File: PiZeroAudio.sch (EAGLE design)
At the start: 66 parts, among them CON1 RPI-ZERO, J1 GROVE, J2 2X2HEADER, J3 2X1-LOCKING, J4 4X1-LOCKING, Q1 DMG2305UX, U1 TXB0104PWR, U2 LSM6DS33, U3 NC7WZ16, U4 DMMT5401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

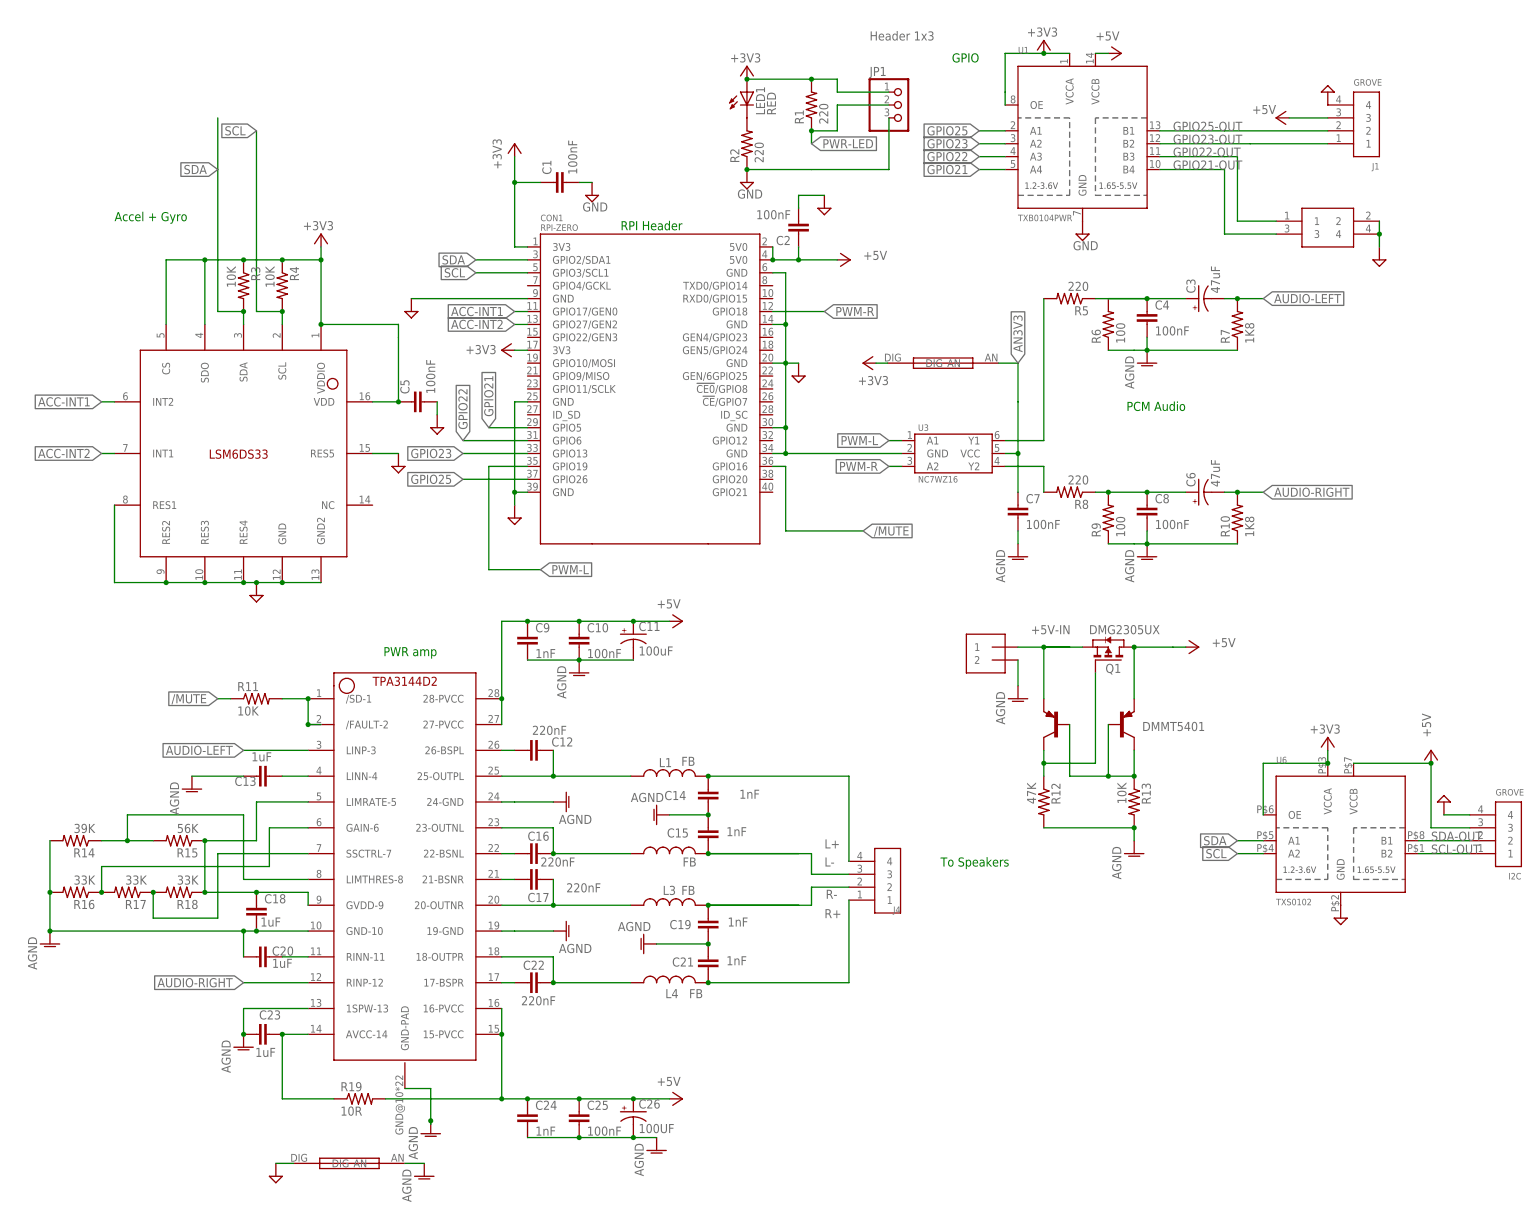
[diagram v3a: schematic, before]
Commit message: Changed capacitor footprints
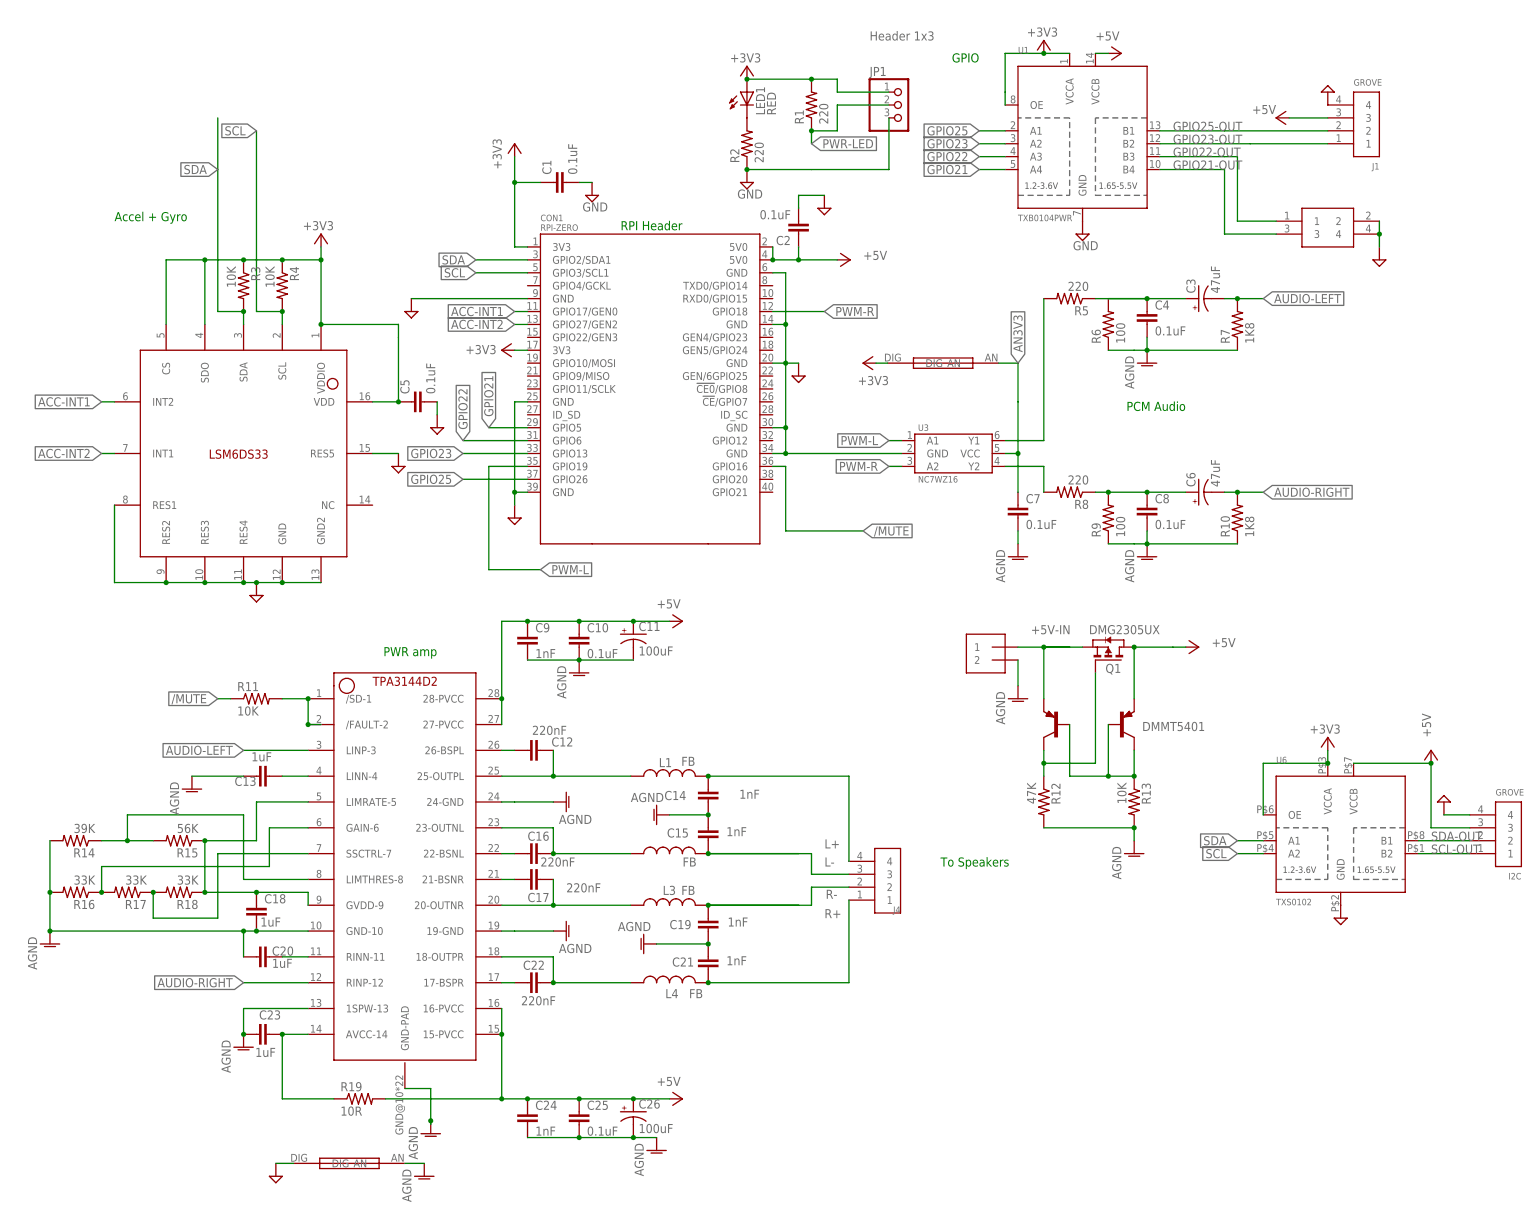
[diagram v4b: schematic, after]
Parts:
- C1, C10, C2, C25, C4, C5, C7, C8: value 100nF -> 0.1uF
- C11, C3, C6: device adafruit:CPOL-USCT3528 -> HappyBrackets:CAP-POLARISED
- C26: value 100UF -> 100uF; device adafruit:CPOL-USCT3528 -> HappyBrackets:CAP-POLARISED
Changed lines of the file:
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@@
 <layer number="112" name="tSilk" color="7" fill="1" visible="yes" active="yes"/>
 <layer number="113" name="IDFDebug" color="7" fill="1" visible="yes" active="yes"/>
+<layer number="114" name="Badge_Outline" color="7" fill="1" visible="no" active="no"/>
+<layer number="115" name="ReferenceISLANDS" color="7" fill="1" visible="no" active="no"/>
 <layer number="116" name="Patch_BOT" color="7" fill="1" visible="yes" active="yes"/>
 <layer number="117" name="mPads" color="7" fill="1" visible="yes" active="yes"/>
@@
 <parts>
 <part name="CON1" library="RPI-Zero" deviceset="RPI-ZERO" device=""/>
-<part name="C4" library="rcl" library_urn="urn:adsk.eagle:library:334" deviceset="C-EU" device="C0603" package3d_urn="urn:adsk.eagle:package:23616/2" value="100nF"/>
-<part name="C8" library="rcl" library_urn="urn:adsk.eagle:library:334" deviceset="C-EU" device="C0603" package3d_urn="urn:adsk.eagle:package:23616/2" value="100nF"/>
-<part name="C3" library="adafruit" deviceset="CPOL-US" device="CT3528" value="47uF"/>
-<part name="C6" library="adafruit" deviceset="CPOL-US" device="CT3528" value="47uF"/>
+<part name="C4" library="rcl" library_urn="urn:adsk.eagle:library:334" deviceset="C-EU" device="C0603" package3d_urn="urn:adsk.eagle:package:23616/2" value="0.1uF"/>
+<part name="C8" library="rcl" library_urn="urn:adsk.eagle:library:334" deviceset="C-EU" device="C0603" package3d_urn="urn:adsk.eagle:package:23616/2" value="0.1uF"/>
+<part name="C3" library="HappyBrackets" library_urn="urn:adsk.eagle:library:5224691" deviceset="CAP-POLARISED" device="" value="47uF"/>
+<part name="C6" library="HappyBrackets" library_urn="urn:adsk.eagle:library:5224691" deviceset="CAP-POLARISED" device="" value="47uF"/>
 <part name="R5" library="adafruit" deviceset="R-US_" device="R0603" value="220"/>
 <part name="R6" library="adafruit" deviceset="R-US_" device="R0603" value="100"/>
@@
 <part name="P+3" library="supply1" library_urn="urn:adsk.eagle:library:371" deviceset="+5V" device=""/>
 <part name="U3" library="fairchild" deviceset="NC7WZ16" device=""/>
-<part name="C7" library="rcl" library_urn="urn:adsk.eagle:library:334" deviceset="C-EU" device="C0603" package3d_urn="urn:adsk.eagle:package:23616/2" value="100nF"/>
+<part name="C7" library="rcl" library_urn="urn:adsk.eagle:library:334" deviceset="C-EU" device="C0603" package3d_urn="urn:adsk.eagle:package:23616/2" value="0.1uF"/>
 <part name="+3V33" library="supply1" library_urn="urn:adsk.eagle:library:371" deviceset="+3V3" device=""/>
 <part name="R7" library="adafruit" deviceset="R-US_" device="R0603" value="1K8"/>
 <part name="R10" library="adafruit" deviceset="R-US_" device="R0603" value="1K8"/>
 <part name="U2" library="HappyBrackets" library_urn="urn:adsk.eagle:library:5224691" deviceset="LSM6DS33" device="LGA-16-3X3" package3d_urn="urn:adsk.eagle:package:5224694/1" value="LSM6DS33"/>
-<part name="C5" library="rcl" library_urn="urn:adsk.eagle:library:334" deviceset="C-EU" device="C0603" package3d_urn="urn:adsk.eagle:package:23616/2" value="100nF"/>
+<part name="C5" library="rcl" library_urn="urn:adsk.eagle:library:334" deviceset="C-EU" device="C0603" package3d_urn="urn:adsk.eagle:package:23616/2" value="0.1uF"/>
 <part name="+3V34" library="supply1" library_urn="urn:adsk.eagle:library:371" deviceset="+3V3" device=""/>
-<part name="C1" library="rcl" library_urn="urn:adsk.eagle:library:334" deviceset="C-EU" device="C0603" package3d_urn="urn:adsk.eagle:package:23616/2" value="100nF"/>
+<part name="C1" library="rcl" library_urn="urn:adsk.eagle:library:334" deviceset="C-EU" device="C0603" package3d_urn="urn:adsk.eagle:package:23616/2" value="0.1uF"/>
 <part name="SUPPLY3" library="supply2" library_urn="urn:adsk.eagle:library:372" deviceset="GND" device=""/>
 <part name="R3" library="adafruit" deviceset="R-US_" device="R0603" value="10K"/>
@@
 <part name="SUPPLY9" library="supply2" library_urn="urn:adsk.eagle:library:372" deviceset="GND" device=""/>
 <part name="SUPPLY12" library="supply2" library_urn="urn:adsk.eagle:library:372" deviceset="GND" device=""/>
-<part name="C2" library="rcl" library_urn="urn:adsk.eagle:library:334" deviceset="C-EU" device="C0603" package3d_urn="urn:adsk.eagle:package:23616/2" value="100nF"/>
+<part name="C2" library="rcl" library_urn="urn:adsk.eagle:library:334" deviceset="C-EU" device="C0603" package3d_urn="urn:adsk.eagle:package:23616/2" value="0.1uF"/>
 <part name="SUPPLY4" library="supply2" library_urn="urn:adsk.eagle:library:372" deviceset="GND" device=""/>
 <part name="U1" library="adafruit" deviceset="TXB0104PWR" device="" value="TXB0104PWR"/>
@@
 <part name="U5" library="HappyBrackets" library_urn="urn:adsk.eagle:library:5224691" deviceset="TPA3144D2PWPR" device="" package3d_urn="urn:adsk.eagle:package:39216/1"/>
 <part name="P+4" library="supply1" library_urn="urn:adsk.eagle:library:371" deviceset="+5V" device=""/>
-<part name="C10" library="rcl" library_urn="urn:adsk.eagle:library:334" deviceset="C-EU" device="C0603" package3d_urn="urn:adsk.eagle:package:23616/2" value="100nF"/>
-<part name="C11" library="adafruit" deviceset="CPOL-US" device="CT3528" value="100uF"/>
+<part name="C10" library="rcl" library_urn="urn:adsk.eagle:library:334" deviceset="C-EU" device="C0603" package3d_urn="urn:adsk.eagle:package:23616/2" value="0.1uF"/>
+<part name="C11" library="HappyBrackets" library_urn="urn:adsk.eagle:library:5224691" deviceset="CAP-POLARISED" device="" value="100uF"/>
 <part name="R11" library="adafruit" deviceset="R-US_" device="R0603" value="10K"/>
 <part name="C13" library="rcl" library_urn="urn:adsk.eagle:library:334" deviceset="C-EU" device="C0603" package3d_urn="urn:adsk.eagle:package:23616/2" value="1uF"/>
@@
 <part name="R19" library="adafruit" deviceset="R-US_" device="R0603" value="10R"/>
 <part name="P+6" library="supply1" library_urn="urn:adsk.eagle:library:371" deviceset="+5V" device=""/>
-<part name="C25" library="rcl" library_urn="urn:adsk.eagle:library:334" deviceset="C-EU" device="C0603" package3d_urn="urn:adsk.eagle:package:23616/2" value="100nF"/>
-<part name="C26" library="adafruit" deviceset="CPOL-US" device="CT3528" value="100UF"/>
+<part name="C25" library="rcl" library_urn="urn:adsk.eagle:library:334" deviceset="C-EU" device="C0603" package3d_urn="urn:adsk.eagle:package:23616/2" value="0.1uF"/>
+<part name="C26" library="HappyBrackets" library_urn="urn:adsk.eagle:library:5224691" deviceset="CAP-POLARISED" device="" value="100uF"/>
 <part name="C24" library="rcl" library_urn="urn:adsk.eagle:library:334" deviceset="C-EU" device="C0603" package3d_urn="urn:adsk.eagle:package:23616/2" value="1nF"/>
 <part name="L1" library="HappyBrackets" library_urn="urn:adsk.eagle:library:5224691" deviceset="NFZ2MSM" device="L0806" package3d_urn="urn:adsk.eagle:package:32724/1" value="FB"/>

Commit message: Changed Capacitor sizes for tant caps
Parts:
- C11, C26, C3, C6: device HappyBrackets:CAP-POLARISED -> HappyBrackets:CAP-POLARISED1206-POLAR
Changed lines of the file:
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@@
 <part name="C4" library="rcl" library_urn="urn:adsk.eagle:library:334" deviceset="C-EU" device="C0603" package3d_urn="urn:adsk.eagle:package:23616/2" value="0.1uF"/>
 <part name="C8" library="rcl" library_urn="urn:adsk.eagle:library:334" deviceset="C-EU" device="C0603" package3d_urn="urn:adsk.eagle:package:23616/2" value="0.1uF"/>
-<part name="C3" library="HappyBrackets" library_urn="urn:adsk.eagle:library:5224691" deviceset="CAP-POLARISED" device="" value="47uF"/>
-<part name="C6" library="HappyBrackets" library_urn="urn:adsk.eagle:library:5224691" deviceset="CAP-POLARISED" device="" value="47uF"/>
+<part name="C3" library="HappyBrackets" library_urn="urn:adsk.eagle:library:5224691" deviceset="CAP-POLARISED" device="1206-POLAR" value="47uF"/>
+<part name="C6" library="HappyBrackets" library_urn="urn:adsk.eagle:library:5224691" deviceset="CAP-POLARISED" device="1206-POLAR" value="47uF"/>
 <part name="R5" library="adafruit" deviceset="R-US_" device="R0603" value="220"/>
 <part name="R6" library="adafruit" deviceset="R-US_" device="R0603" value="100"/>
@@
 <part name="P+4" library="supply1" library_urn="urn:adsk.eagle:library:371" deviceset="+5V" device=""/>
 <part name="C10" library="rcl" library_urn="urn:adsk.eagle:library:334" deviceset="C-EU" device="C0603" package3d_urn="urn:adsk.eagle:package:23616/2" value="0.1uF"/>
-<part name="C11" library="HappyBrackets" library_urn="urn:adsk.eagle:library:5224691" deviceset="CAP-POLARISED" device="" value="100uF"/>
+<part name="C11" library="HappyBrackets" library_urn="urn:adsk.eagle:library:5224691" deviceset="CAP-POLARISED" device="1206-POLAR" value="100uF"/>
 <part name="R11" library="adafruit" deviceset="R-US_" device="R0603" value="10K"/>
 <part name="C13" library="rcl" library_urn="urn:adsk.eagle:library:334" deviceset="C-EU" device="C0603" package3d_urn="urn:adsk.eagle:package:23616/2" value="1uF"/>
@@
 <part name="P+6" library="supply1" library_urn="urn:adsk.eagle:library:371" deviceset="+5V" device=""/>
 <part name="C25" library="rcl" library_urn="urn:adsk.eagle:library:334" deviceset="C-EU" device="C0603" package3d_urn="urn:adsk.eagle:package:23616/2" value="0.1uF"/>
-<part name="C26" library="HappyBrackets" library_urn="urn:adsk.eagle:library:5224691" deviceset="CAP-POLARISED" device="" value="100uF"/>
+<part name="C26" library="HappyBrackets" library_urn="urn:adsk.eagle:library:5224691" deviceset="CAP-POLARISED" device="1206-POLAR" value="100uF"/>
 <part name="C24" library="rcl" library_urn="urn:adsk.eagle:library:334" deviceset="C-EU" device="C0603" package3d_urn="urn:adsk.eagle:package:23616/2" value="1nF"/>
 <part name="L1" library="HappyBrackets" library_urn="urn:adsk.eagle:library:5224691" deviceset="NFZ2MSM" device="L0806" package3d_urn="urn:adsk.eagle:package:32724/1" value="FB"/>

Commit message: Changed the name of RPI Header
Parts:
- CON1: value RPI-ZERO -> RPI-Header
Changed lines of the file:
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@@
 </classes>
 <parts>
-<part name="CON1" library="RPI-Zero" deviceset="RPI-ZERO" device=""/>
+<part name="CON1" library="RPI-Zero" deviceset="RPI-ZERO" device="" value="RPI-Header"/>
 <part name="C4" library="rcl" library_urn="urn:adsk.eagle:library:334" deviceset="C-EU" device="C0603" package3d_urn="urn:adsk.eagle:package:23616/2" value="0.1uF"/>
 <part name="C8" library="rcl" library_urn="urn:adsk.eagle:library:334" deviceset="C-EU" device="C0603" package3d_urn="urn:adsk.eagle:package:23616/2" value="0.1uF"/>

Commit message: Swapped position of Mosfet Capacitively coupled Audio Set OE of I2C translator to GND Set Mute so it floats to +5
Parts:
- removed R12: 47K, adafruit:R-US_R0603
- removed R13: 10K, adafruit:R-US_R0603
- removed U4: DMMT5401, HappyBrackets:DMMT5401
- added C27, C28: 1uF, rcl:C-EUC0603
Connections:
- removed net N$22: R13.1, U4G$1.B, U4G$2.B, U4G$2.C
- removed net N$27: Q1.G, R12.1, U4G$1.C
- new net N$11: C28.1, U5.RINP-12
- new net OE: CON1.GPIO20, U1.OE
- net +3V3: no longer U1.OE, U6.OE
- net +5V: now also Q1.S, R11.1; no longer Q1.D, U4G$2.E
- net +5V-IN: now also Q1.D; no longer Q1.S, U4G$1.E
- net /MUTE: now also R11.2, U5./FAULT-2, U5./SD-1; no longer R11.1
- net AGND: now also Q1.G; no longer R12.2, R13.2
- net AUDIO-LEFT: now also C27.2; no longer U5.LINP-3
- net AUDIO-RIGHT: now also C28.2; no longer U5.RINP-12
- net GND: now also U6.OE
- net N$5: now also C27.1, U5.LINP-3; no longer R11.2, U5./FAULT-2, U5./SD-1
